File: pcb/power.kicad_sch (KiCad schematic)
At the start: 4 parts, among them U3 TPS613226ADBVR

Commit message: Swap to STC8H1K08 and work on JLCPCB assembly support
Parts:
- C1: LCSC (none) -> C59461
- L1: LCSC (none) -> C42215
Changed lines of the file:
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@@
+			)
+		)
+		(property "LCSC" "C59461"
+			(at 100.33 73.66 0)
+			(effects
+				(font
+					(size 1.27 1.27)
+				)
+				(hide yes)
 			)
 		)
@@
 			(at 60.96 69.85 0)
 			(effects
+				(font
+					(size 1.27 1.27)
+				)
+				(hide yes)
+			)
+		)
+		(property "LCSC" "C42215"
+			(at 60.96 69.85 0)
+			(effects

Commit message: More edits to PCB design
 - Change a couple of parts - voltage regulator - to use LCSC parts
 - Increase width of the nametag PCB
 - redo layout a bit
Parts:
- removed U3: TPS613226ADBVR, Package_TO_SOT_SMD:SOT-23-5, symbol Regulator_Switching:TPS613226ADBV
- added U2: BL8536CB3TR36, Package_TO_SOT_SMD:SOT-23, symbol lcsc:BL8536CB3TR36
- BT1: value Keystone Electronics 2466 -> C5290189
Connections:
- net +3.3V: now also U2.3 (VOUT)
- net GND: now also U2.1 (GND)
- net at L1.2: now also U2.2 (SW)

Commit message: Small changes for manufacturability
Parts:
- L1: footprint Inductor_SMD:L_0805_2012Metric_Pad1.15x1.40mm_HandSolder -> Inductor_SMD:L_Wuerth_PMFI-201610_PMCI-compatible
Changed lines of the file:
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@@
 			)
 		)
-		(property "Footprint" "Inductor_SMD:L_0805_2012Metric_Pad1.15x1.40mm_HandSolder"
+		(property "Footprint" "Inductor_SMD:L_Wuerth_PMFI-201610_PMCI-compatible"
 			(at 60.96 69.85 0)
 			(hide yes)

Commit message: Update footprints from LCSC EasyEDA Library
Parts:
- BT1: value C5290189 -> BH-AAA-A1AJ001; footprint Battery:BatteryHolder_Keystone_2466_1xAAA -> EasyEDA:BAT-TH_BH-AAA-A1AJ001; symbol Device:Battery_Cell -> EasyEDA:BH-AAA-A1AJ001; LCSC (none) -> C5290189; LCSC Part (none) -> C5290189; MPN (none) -> BH-AAA-A1AJ001; Manufacturer (none) -> MYOUNG(美阳)
- L1: footprint Inductor_SMD:L_Wuerth_PMFI-201610_PMCI-compatible -> EasyEDA:L0806
- U2: footprint Package_TO_SOT_SMD:SOT-23 -> EasyEDA:SOT-23-3_L2.9-W1.6-P1.90-LS2.8-BR
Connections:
- net GND: now also BT1.1 (-); no longer BT1.2 (-)
- net at L1.1: now also BT1.2 (+); no longer BT1.1 (+)
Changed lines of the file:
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@@
 			)
 		)
-		(property "Footprint" "Package_TO_SOT_SMD:SOT-23"
+		(property "Footprint" "EasyEDA:SOT-23-3_L2.9-W1.6-P1.90-LS2.8-BR"
 			(at 81.28 92.71 0)
 			(hide yes)
@@
 			)
 		)
-		(property "Footprint" "Inductor_SMD:L_Wuerth_PMFI-201610_PMCI-compatible"
+		(property "Footprint" "EasyEDA:L0806"
 			(at 60.96 69.85 0)
 			(hide yes)
@@
 	(symbol
 		(lib_id "power:GND")
-		(at 45.72 77.47 0)
+		(at 45.72 80.01 0)
 		(unit 1)
 		(body_style 1)
@@
 		(fields_autoplaced yes)
 		(property "Reference" "#PWR01"
-			(at 45.72 83.82 0)
+			(at 45.72 86.36 0)
 			(hide yes)
 			(show_name no)
@@
 		)
 		(property "Value" "GND"
-			(at 45.72 81.6031 0)
+			(at 45.72 84.1431 0)
 			(show_name no)
 			(do_not_autoplace no)
@@
 		)
 		(property "Footprint" ""
-			(at 45.72 77.47 0)
+			(at 45.72 80.01 0)
 			(hide yes)
 			(show_name no)
@@
 		)
 		(property "Datasheet" ""
-			(at 45.72 77.47 0)
+			(at 45.72 80.01 0)
 			(hide yes)
 			(show_name no)
@@
 		)
 		(property "Description" "Power symbol creates a global label with name \"GND\" , ground"
-			(at 45.72 77.47 0)
+			(at 45.72 80.01 0)
 			(hide yes)
 			(show_name no)
@@
 	)
 	(symbol
-		(lib_id "Device:Battery_Cell")
-		(at 45.72 74.93 0)
+		(lib_id "EasyEDA:BH-AAA-A1AJ001")
+		(at 45.72 74.93 270)
 		(unit 1)
 		(body_style 1)
@@
 		(fields_autoplaced yes)
 		(property "Reference" "BT1"
-			(at 48.641 71.8763 0)
+			(at 50.165 73.7178 90)
 			(show_name no)
 			(do_not_autoplace no)
@@
 			)
 		)
-		(property "Value" "C5290189"
-			(at 48.641 74.3006 0)
+		(property "Value" "BH-AAA-A1AJ001"
+			(at 50.165 76.1421 90)
 			(show_name no)
 			(do_not_autoplace no)
@@
 			)
 		)
-		(property "Footprint" "Battery:BatteryHolder_Keystone_2466_1xAAA"
-			(at 45.72 73.406 90)
-			(hide yes)
-			(show_name no)
-			(do_not_autoplace no)
-			(effects
-				(font
-					(size 1.27 1.27)
-				)
-			)
-		)
-		(property "Datasheet" ""
-			(at 45.72 73.406 90)
+		(property "Footprint" "EasyEDA:BAT-TH_BH-AAA-A1AJ001"
+			(at 38.1 74.93 0)
+			(hide yes)
+			(show_name no)
+			(do_not_autoplace no)
+			(effects
+				(font
+					(size 1.27 1.27)
+				)
+			)
+		)
+		(property "Datasheet" "https://www.lcsc.com/datasheet/C5290189.pdf"
+			(at 35.56 74.93 0)
 			(hide yes)
 			(show_name no)
@@
 			(hide yes)
 			(show_name no)
+			(do_not_autoplace no)
+			(effects
+				(font
+					(size 1.27 1.27)
+				)
+			)
+		)
+		(property "LCSC" "C5290189"
+			(at 45.72 74.93 0)
+			(hide yes)
+			(show_name no)
+			(do_not_autoplace no)
+			(effects
+				(font
+					(size 1.27 1.27)
+				)
+			)
+		)
+		(property "Manufacturer" "MYOUNG(美阳)"
+			(at 33.02 74.93 0)
+			(hide yes)
+			(show_name no)
+			(do_not_autoplace no)
+			(effects
+				(font
+					(size 1.27 1.27)
+				)
+			)
+		)
+		(property "MPN" "BH-AAA-A1AJ001"
+			(at 30.48 74.93 0)
+			(hide yes)
+			(show_name no)
+			(do_not_autoplace no)
+			(effects
+				(font
+					(size 1.27 1.27)
+				)
+			)
+		)
+		(property "LCSC Part" "C5290189"
+			(at 27.94 74.93 0)
+			(hide yes)
+			(show_name no)

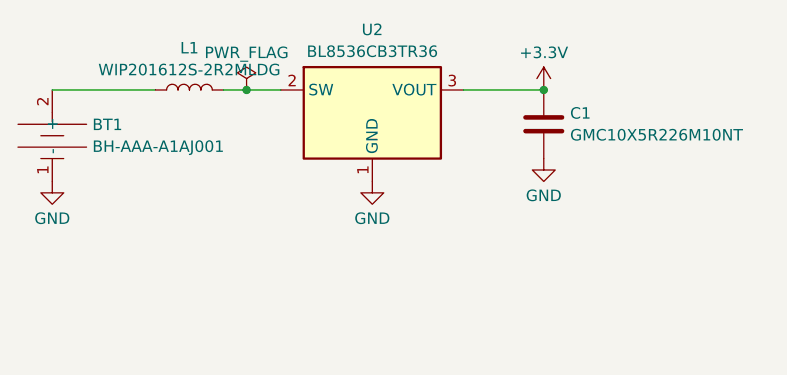
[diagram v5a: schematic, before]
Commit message: Redo some of the layout, move button
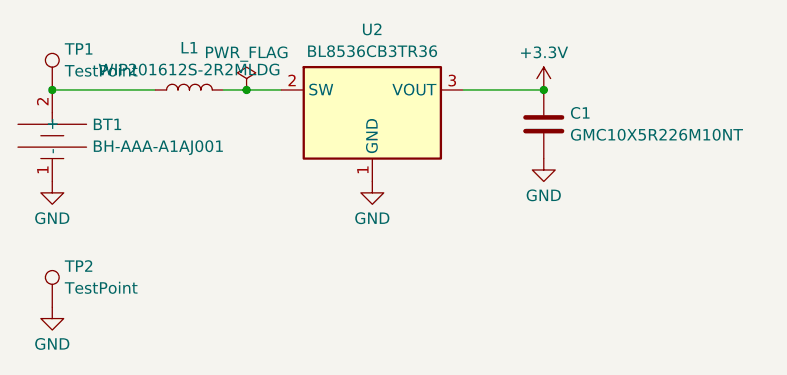
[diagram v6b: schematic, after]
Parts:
- added TP1, TP2: TestPoint, TestPoint:TestPoint_Pad_D1.0mm, symbol Connector:TestPoint
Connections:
- net GND: now also TP2.1
- net at BT1.2 (+), L1.1: now also TP1.1
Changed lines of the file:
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@@
+	)
+	(junction
+		(at 45.72 69.85)
+		(diameter 0)
+		(color 0 0 0 0)
 	)
 	(junction
@@
 	)
 	(symbol
+		(lib_id "Connector:TestPoint")
+		(at 45.72 69.85 0)
+		(unit 1)
+		(body_style 1)
+		(exclude_from_sim no)
+		(in_bom yes)
+		(on_board yes)
+		(in_pos_files yes)
+		(dnp no)
+		(fields_autoplaced yes)
+		(property "Reference" "TP1"
+			(at 47.117 65.3358 0)
+			(show_name no)
+			(do_not_autoplace no)
+			(effects
+				(font
+					(size 1.27 1.27)
+				)
+				(justify left)
+			)
+		)
+		(property "Value" "TestPoint"
+			(at 47.117 67.7601 0)
+			(show_name no)
+			(do_not_autoplace no)
+			(effects
+				(font
+					(size 1.27 1.27)
+				)
+				(justify left)
+			)
+		)
+		(property "Footprint" "TestPoint:TestPoint_Pad_D1.0mm"
+			(at 50.8 69.85 0)
+			(hide yes)
+			(show_name no)
+			(do_not_autoplace no)
+			(effects
+				(font
+					(size 1.27 1.27)
+				)
+			)
+		)
+		(property "Datasheet" ""
+			(at 50.8 69.85 0)
+			(hide yes)
+			(show_name no)
+			(do_not_autoplace no)
+			(effects
+				(font
+					(size 1.27 1.27)
+				)
+			)
+		)
+		(property "Description" "test point"
+			(at 45.72 69.85 0)
+			(hide yes)
+			(show_name no)
+			(do_not_autoplace no)
+			(effects
+				(font
+					(size 1.27 1.27)
+				)
+			)
+		)
+		(pin "1"
+		)
+		(instances
+			(project "nametag"
+				(path "/a7c50b29-e914-4aee-9ec8-81f37f7bd068/a48f65a2-3369-4655-9ad9-13ca4e244bfb"
+					(reference "TP1")
+					(unit 1)
+				)
+			)
+		)
+	)
+	(symbol
 		(lib_id "power:PWR_FLAG")
 		(at 67.31 69.85 0)
@@
 					(unit 1)
 				)
+			)
+		)
+	)
+	(symbol
+		(lib_id "Connector:TestPoint")
+		(at 45.72 93.98 0)
+		(unit 1)
+		(body_style 1)
+		(exclude_from_sim no)
+		(in_bom yes)
+		(on_board yes)
+		(in_pos_files yes)
+		(dnp no)
+		(fields_autoplaced yes)
+		(property "Reference" "TP2"
+			(at 47.117 89.4658 0)
+			(show_name no)
+			(do_not_autoplace no)
+			(effects
+				(font
+					(size 1.27 1.27)
+				)
+				(justify left)
+			)
+		)
+		(property "Value" "TestPoint"
+			(at 47.117 91.8901 0)
+			(show_name no)
+			(do_not_autoplace no)
+			(effects
+				(font
+					(size 1.27 1.27)
+				)
+				(justify left)
+			)
+		)
+		(property "Footprint" "TestPoint:TestPoint_Pad_D1.0mm"
+			(at 50.8 93.98 0)
+			(hide yes)
+			(show_name no)
+			(do_not_autoplace no)
+			(effects
+				(font
+					(size 1.27 1.27)
+				)
+			)
+		)
+		(property "Datasheet" ""
+			(at 50.8 93.98 0)
+			(hide yes)
+			(show_name no)
+			(do_not_autoplace no)
+			(effects
+				(font
+					(size 1.27 1.27)
+				)
+			)
+		)
+		(property "Description" "test point"
+			(at 45.72 93.98 0)
+			(hide yes)
+			(show_name no)
+			(do_not_autoplace no)
+			(effects
+				(font
+					(size 1.27 1.27)
+				)
+			)
+		)
+		(pin "1"
+		)
+		(instances
+			(project "nametag"
+				(path "/a7c50b29-e914-4aee-9ec8-81f37f7bd068/a48f65a2-3369-4655-9ad9-13ca4e244bfb"
+					(reference "TP2")
+					(unit 1)
+				)
+			)
+		)
+	)
+	(symbol
+		(lib_id "power:GND")
+		(at 45.72 93.98 0)
+		(unit 1)
+		(body_style 1)
+		(exclude_from_sim no)
+		(in_bom yes)
+		(on_board yes)
+		(in_pos_files yes)
+		(dnp no)
+		(fields_autoplaced yes)
+		(property "Reference" "#PWR010"
+			(at 45.72 100.33 0)
+			(hide yes)
+			(show_name no)
+			(do_not_autoplace no)
+			(effects
+				(font
+					(size 1.27 1.27)
+				)
+			)
+		)
+		(property "Value" "GND"
+			(at 45.72 98.1131 0)
+			(show_name no)
+			(do_not_autoplace no)
+			(effects
+				(font
+					(size 1.27 1.27)
+				)
+			)
+		)
+		(property "Footprint" ""
+			(at 45.72 93.98 0)
+			(hide yes)
+			(show_name no)
+			(do_not_autoplace no)
+			(effects
+				(font
+					(size 1.27 1.27)
+				)
+			)
+		)
+		(property "Datasheet" ""
+			(at 45.72 93.98 0)
+			(hide yes)
+			(show_name no)
+			(do_not_autoplace no)
+			(effects
+				(font
+					(size 1.27 1.27)
+				)
+			)
+		)
+		(property "Description" "Power symbol creates a global label with name \"GND\" , ground"
+			(at 45.72 93.98 0)
+			(hide yes)
+			(show_name no)
+			(do_not_autoplace no)
+			(effects
+				(font
+					(size 1.27 1.27)
+				)
+			)
+		)
+		(pin "1"
+		)
+		(instances
+			(project "nametag"
+				(path "/a7c50b29-e914-4aee-9ec8-81f37f7bd068/a48f65a2-3369-4655-9ad9-13ca4e244bfb"
+					(reference "#PWR010")
+					(unit 1)
+				)

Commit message: Submit files to JLCPCB for manufacture
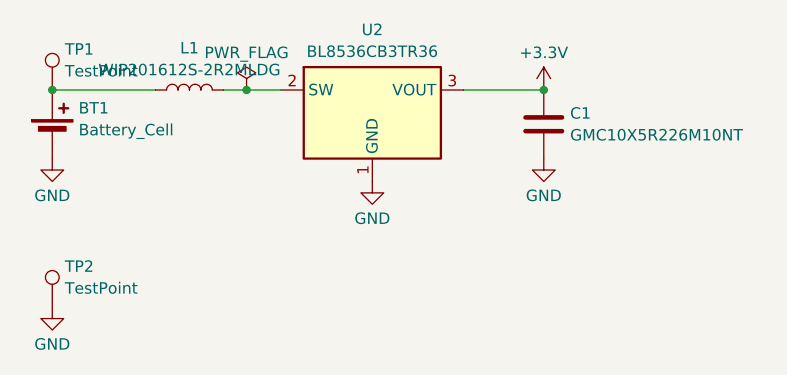
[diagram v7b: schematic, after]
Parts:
- removed BT1: BH-AAA-A1AJ001, EasyEDA:BAT-TH_BH-AAA-A1AJ001, symbol EasyEDA:BH-AAA-A1AJ001
- added BT1: Battery_Cell, Battery:BatteryHolder_Keystone_2466_1xAAA, symbol Device:Battery_Cell
- C1: footprint Capacitor_SMD:C_0603_1608Metric_Pad1.08x0.95mm_HandSolder -> Capacitor_SMD:C_0603_1608Metric
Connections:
- net GND: now also BT1.2 (-)
- net at L1.1, TP1.1: now also BT1.1 (+)
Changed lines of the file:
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@@
+	)
+	(symbol
+		(lib_id "Device:Battery_Cell")
+		(at 45.72 74.93 0)
+		(unit 1)
+		(body_style 1)
+		(exclude_from_sim no)
+		(in_bom yes)
+		(on_board yes)
+		(in_pos_files yes)
+		(dnp no)
+		(fields_autoplaced yes)
+		(property "Reference" "BT1"
+			(at 48.641 71.8763 0)
+			(show_name no)
+			(do_not_autoplace no)
+			(effects
+				(font
+					(size 1.27 1.27)
+				)
+				(justify left)
+			)
+		)
+		(property "Value" "Battery_Cell"
+			(at 48.641 74.3006 0)
+			(show_name no)
+			(do_not_autoplace no)
+			(effects
+				(font
+					(size 1.27 1.27)
+				)
+				(justify left)
+			)
+		)
+		(property "Footprint" "Battery:BatteryHolder_Keystone_2466_1xAAA"
+			(at 45.72 73.406 90)
+			(hide yes)
+			(show_name no)
+			(do_not_autoplace no)
+			(effects
+				(font
+					(size 1.27 1.27)
+				)
+			)
+		)
+		(property "Datasheet" ""
+			(at 45.72 73.406 90)
+			(hide yes)
+			(show_name no)
+			(do_not_autoplace no)
+			(effects
+				(font
+					(size 1.27 1.27)
+				)
+			)
+		)
+		(property "Description" "Single-cell battery"
+			(at 45.72 74.93 0)
+			(hide yes)
+			(show_name no)
+			(do_not_autoplace no)
+			(effects
+				(font
+					(size 1.27 1.27)
+				)
+			)
+		)
+		(property "Sim.Device" "V"
+			(at 45.72 74.93 0)
+			(hide yes)
+			(show_name no)
+			(do_not_autoplace no)
+			(effects
+				(font
+					(size 1.27 1.27)
+				)
+			)
+		)
+		(property "Sim.Type" "DC"
+			(at 45.72 74.93 0)
+			(hide yes)
+			(show_name no)
+			(do_not_autoplace no)
+			(effects
+				(font
+					(size 1.27 1.27)
+				)
+			)
+		)
+		(property "Sim.Pins" "1=+ 2=-"
+			(at 45.72 74.93 0)
+			(hide yes)
+			(show_name no)
+			(do_not_autoplace no)
+			(effects
+				(font
+					(size 1.27 1.27)
+				)
+			)
+		)
+		(pin "1"
+		)
+		(pin "2"
+		)
+		(instances
+			(project "nametag"
+				(path "/a7c50b29-e914-4aee-9ec8-81f37f7bd068/a48f65a2-3369-4655-9ad9-13ca4e244bfb"
+					(reference "BT1")
+					(unit 1)
+				)
+			)
+		)
 	)
 	(symbol
@@
 			)
 		)
-		(property "Footprint" "Capacitor_SMD:C_0603_1608Metric_Pad1.08x0.95mm_HandSolder"
+		(property "Footprint" "Capacitor_SMD:C_0603_1608Metric"
 			(at 101.2952 77.47 0)
 			(hide yes)
@@
 	(symbol
 		(lib_id "power:GND")
-		(at 45.72 80.01 0)
+		(at 45.72 77.47 0)
 		(unit 1)
 		(body_style 1)
@@
 		(fields_autoplaced yes)
 		(property "Reference" "#PWR01"
-			(at 45.72 86.36 0)
+			(at 45.72 83.82 0)
 			(hide yes)
 			(show_name no)
@@
 		)
 		(property "Value" "GND"
-			(at 45.72 84.1431 0)
+			(at 45.72 81.6031 0)
 			(show_name no)
 			(do_not_autoplace no)
@@
 		)
 		(property "Footprint" ""
-			(at 45.72 80.01 0)
-			(hide yes)
-			(show_name no)
-			(do_not_autoplace no)
-			(effects
-				(font
-					(size 1.27 1.27)
-				)
-			)
-		)
-		(property "Datasheet" ""
-			(at 45.72 80.01 0)
+			(at 45.72 77.47 0)
+			(hide yes)
+			(show_name no)
+			(do_not_autoplace no)
+			(effects
+				(font
+					(size 1.27 1.27)
+				)
+			)
+		)
+		(property "Datasheet" ""
+			(at 45.72 77.47 0)
 			(hide yes)
 			(show_name no)
@@
 		)
 		(property "Description" "Power symbol creates a global label with name \"GND\" , ground"
-			(at 45.72 80.01 0)
+			(at 45.72 77.47 0)
 			(hide yes)
 			(show_name no)
@@
 					(unit 1)
 				)
-			)
-		)
-	)
-	(symbol
-		(lib_id "EasyEDA:BH-AAA-A1AJ001")
-		(at 45.72 74.93 270)
-		(unit 1)
-		(body_style 1)
-		(exclude_from_sim no)
-		(in_bom yes)
-		(on_board yes)
-		(in_pos_files yes)
-		(dnp no)
-		(fields_autoplaced yes)
-		(property "Reference" "BT1"
-			(at 50.165 73.7178 90)
-			(show_name no)
-			(do_not_autoplace no)
-			(effects
-				(font
-					(size 1.27 1.27)
-				)
-				(justify left)
-			)
-		)
-		(property "Value" "BH-AAA-A1AJ001"
-			(at 50.165 76.1421 90)
-			(show_name no)
-			(do_not_autoplace no)
-			(effects
-				(font
-					(size 1.27 1.27)
-				)
-				(justify left)
-			)
-		)
-		(property "Footprint" "EasyEDA:BAT-TH_BH-AAA-A1AJ001"
-			(at 38.1 74.93 0)
-			(hide yes)
-			(show_name no)
-			(do_not_autoplace no)
-			(effects
-				(font
-					(size 1.27 1.27)
-				)
-			)
-		)
-		(property "Datasheet" "https://www.lcsc.com/datasheet/C5290189.pdf"
-			(at 35.56 74.93 0)
-			(hide yes)
-			(show_name no)
-			(do_not_autoplace no)
-			(effects
-				(font
-					(size 1.27 1.27)
-				)
-			)
-		)
-		(property "Description" "Single-cell battery"
-			(at 45.72 74.93 0)
-			(hide yes)
-			(show_name no)
-			(do_not_autoplace no)
-			(effects
-				(font
-					(size 1.27 1.27)
-				)
-			)
-		)
-		(property "Sim.Device" "V"
-			(at 45.72 74.93 0)
-			(hide yes)
-			(show_name no)
-			(do_not_autoplace no)
-			(effects
-				(font
-					(size 1.27 1.27)
-				)
-			)
-		)
-		(property "Sim.Type" "DC"
-			(at 45.72 74.93 0)
-			(hide yes)
-			(show_name no)
-			(do_not_autoplace no)
-			(effects
-				(font
-					(size 1.27 1.27)
-				)
-			)
-		)
-		(property "Sim.Pins" "1=+ 2=-"
-			(at 45.72 74.93 0)
-			(hide yes)
-			(show_name no)
-			(do_not_autoplace no)
-			(effects
-				(font
-					(size 1.27 1.27)
-				)
-			)
-		)
-		(property "LCSC" "C5290189"
-			(at 45.72 74.93 0)
-			(hide yes)
-			(show_name no)
-			(do_not_autoplace no)
-			(effects
-				(font
-					(size 1.27 1.27)
-				)
-			)
-		)
-		(property "Manufacturer" "MYOUNG(美阳)"
-			(at 33.02 74.93 0)
-			(hide yes)
-			(show_name no)
-			(do_not_autoplace no)
-			(effects
-				(font
-					(size 1.27 1.27)
-				)
-			)
-		)
-		(property "MPN" "BH-AAA-A1AJ001"
-			(at 30.48 74.93 0)
-			(hide yes)
-			(show_name no)
-			(do_not_autoplace no)
-			(effects
-				(font
-					(size 1.27 1.27)
-				)
-			)
-		)
-		(property "LCSC Part" "C5290189"
-			(at 27.94 74.93 0)
-			(hide yes)
-			(show_name no)
-			(do_not_autoplace no)
-			(effects
-				(font
-					(size 1.27 1.27)
-				)
-			)
-		)
-		(pin "2"
-		)
-		(pin "1"
-		)
-		(instances
-			(project "nametag"
-				(path "/a7c50b29-e914-4aee-9ec8-81f37f7bd068/a48f65a2-3369-4655-9ad9-13ca4e244bfb"
-					(reference "BT1")
-					(unit 1)
-				)
